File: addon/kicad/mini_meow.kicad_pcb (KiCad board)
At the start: 2 copper layers, 49.3 x 63.4 mm, 13 parts, among them U1 sa_connector

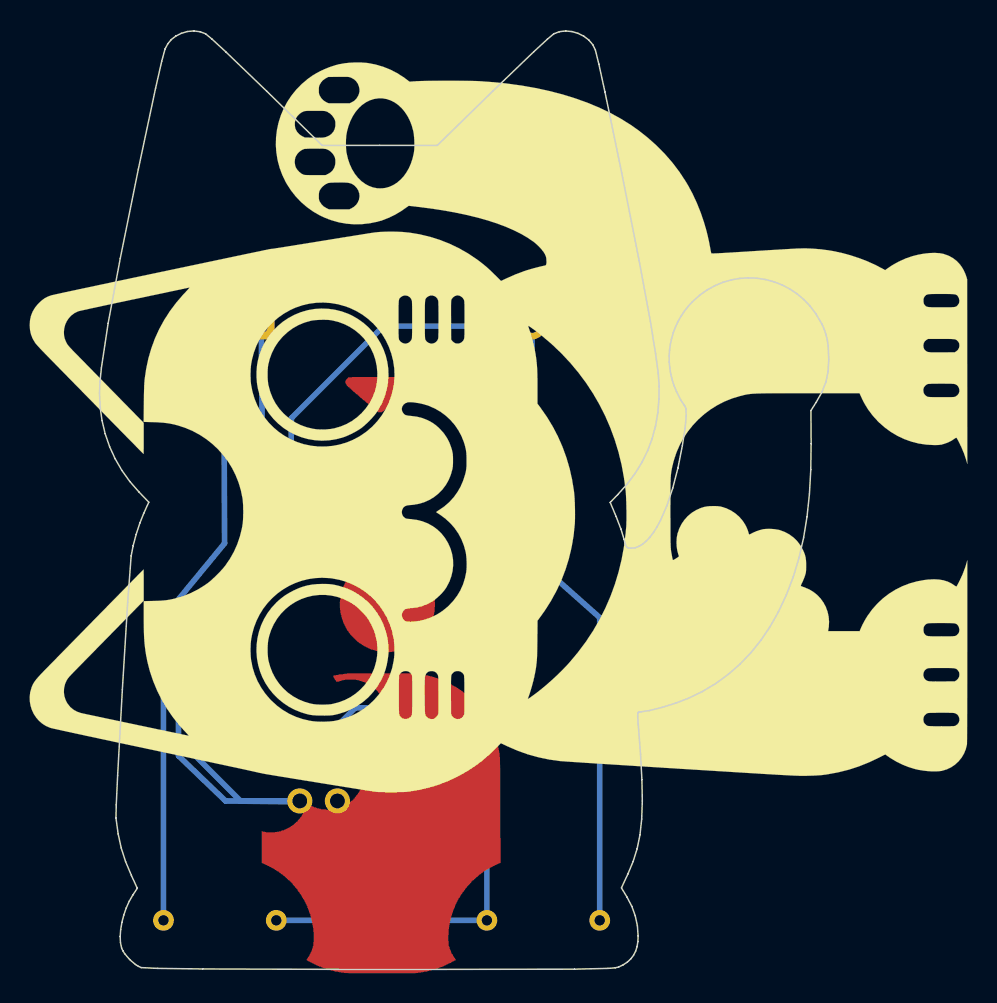
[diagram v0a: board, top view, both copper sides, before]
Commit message: updated kicad to display layers and fix silk rotation
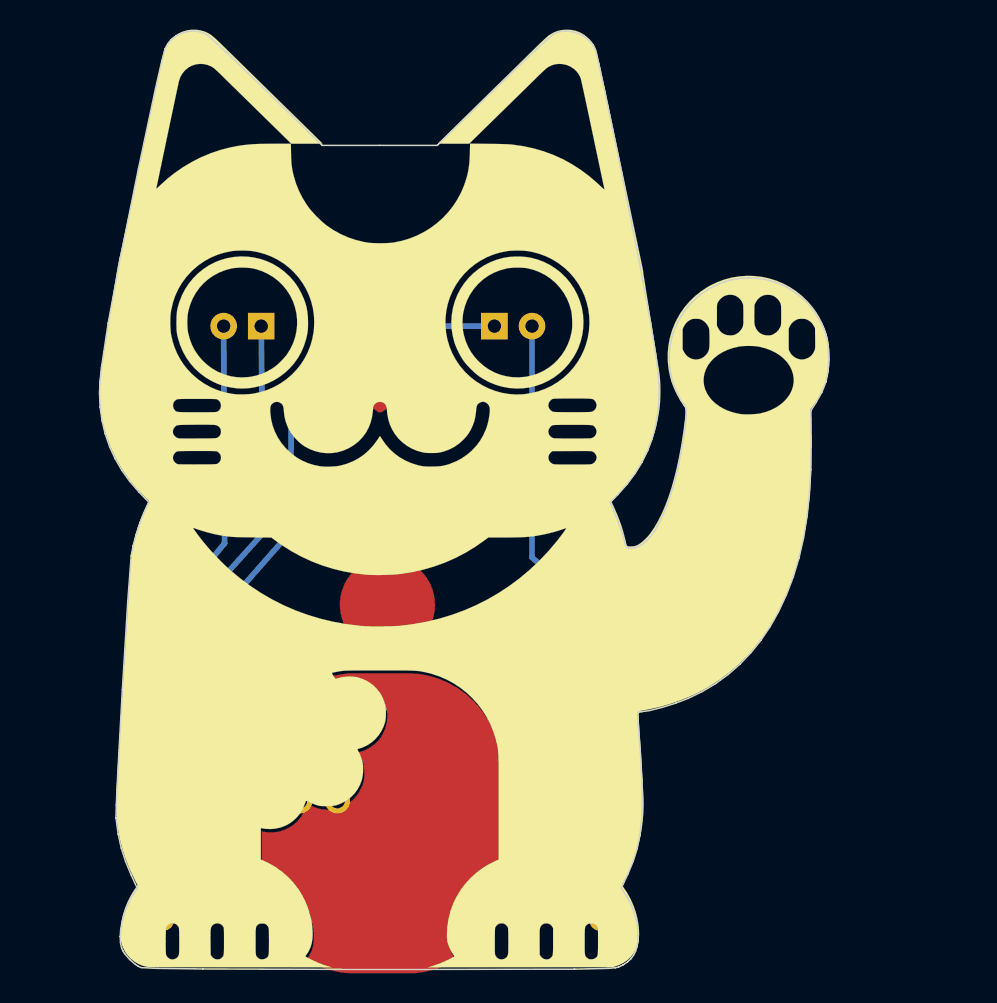
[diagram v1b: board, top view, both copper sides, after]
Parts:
- moved G*** 1.51 mm to (152.1, 88.6), turned to 0 degrees
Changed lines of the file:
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@@
   (page A4)
   (layers
-    (0 F.Cu signal hide)
+    (0 F.Cu signal)
     (31 B.Cu signal)
     (32 B.Adhes user hide)
@@
     (35 F.Paste user hide)
     (36 B.SilkS user)
-    (37 F.SilkS user hide)
-    (38 B.Mask user hide)
-    (39 F.Mask user hide)
-    (40 Dwgs.User user hide)
+    (37 F.SilkS user)
+    (38 B.Mask user)
+    (39 F.Mask user)
+    (40 Dwgs.User user)
     (41 Cmts.User user)
     (42 Eco1.User user)
@@
   )
   (module mini_meow:mini_meow_silk_lg (layer F.Cu)
-    (at 152.9715 89.916 90)
-    (fp_text reference G*** (at 0 0 90) (layer F.SilkS) hide
+    (at 152.146 88.646)
+    (fp_text reference G*** (at 0 0) (layer F.SilkS) hide
       (effects (font (thickness 0.3)))
     )
-    (fp_text value LOGO (at 0.75 0 90) (layer F.SilkS) hide
+    (fp_text value LOGO (at 0.75 0) (layer F.SilkS) hide
       (effects (font (thickness 0.3)))
     )
@@
   (gr_line (start 132.607035 124.095547) (end 132.41897 124.01002) (layer Edge.Cuts) (width 0.1))
   (segment (start 148.971 80.772) (end 148.971 80.772) (width 0.381) (layer B.Cu) (net 1))
-  (segment (start 156.464 80.772) (end 148.971 80.772) (width 0.381) (layer B.Cu) (net 1) (status 400000))
+  (segment (start 156.464 80.772) (end 148.971 80.772) (width 0.381) (layer B.Cu) (net 1))
   (segment (start 142.746876 86.996124) (end 148.971 80.772) (width 0.381) (layer B.Cu) (net 1))
   (segment (start 143.3195 112.8395) (end 139.319 112.8395) (width 0.381) (layer B.Cu) (net 1))
